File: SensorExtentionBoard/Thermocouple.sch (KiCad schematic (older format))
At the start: 9 parts, among them J301 Conn_01x02_Male, J302 Conn_01x02_Male, U301 MCP4728, U302 TS3A24159DGSR, U303 TS3A24159DGSR

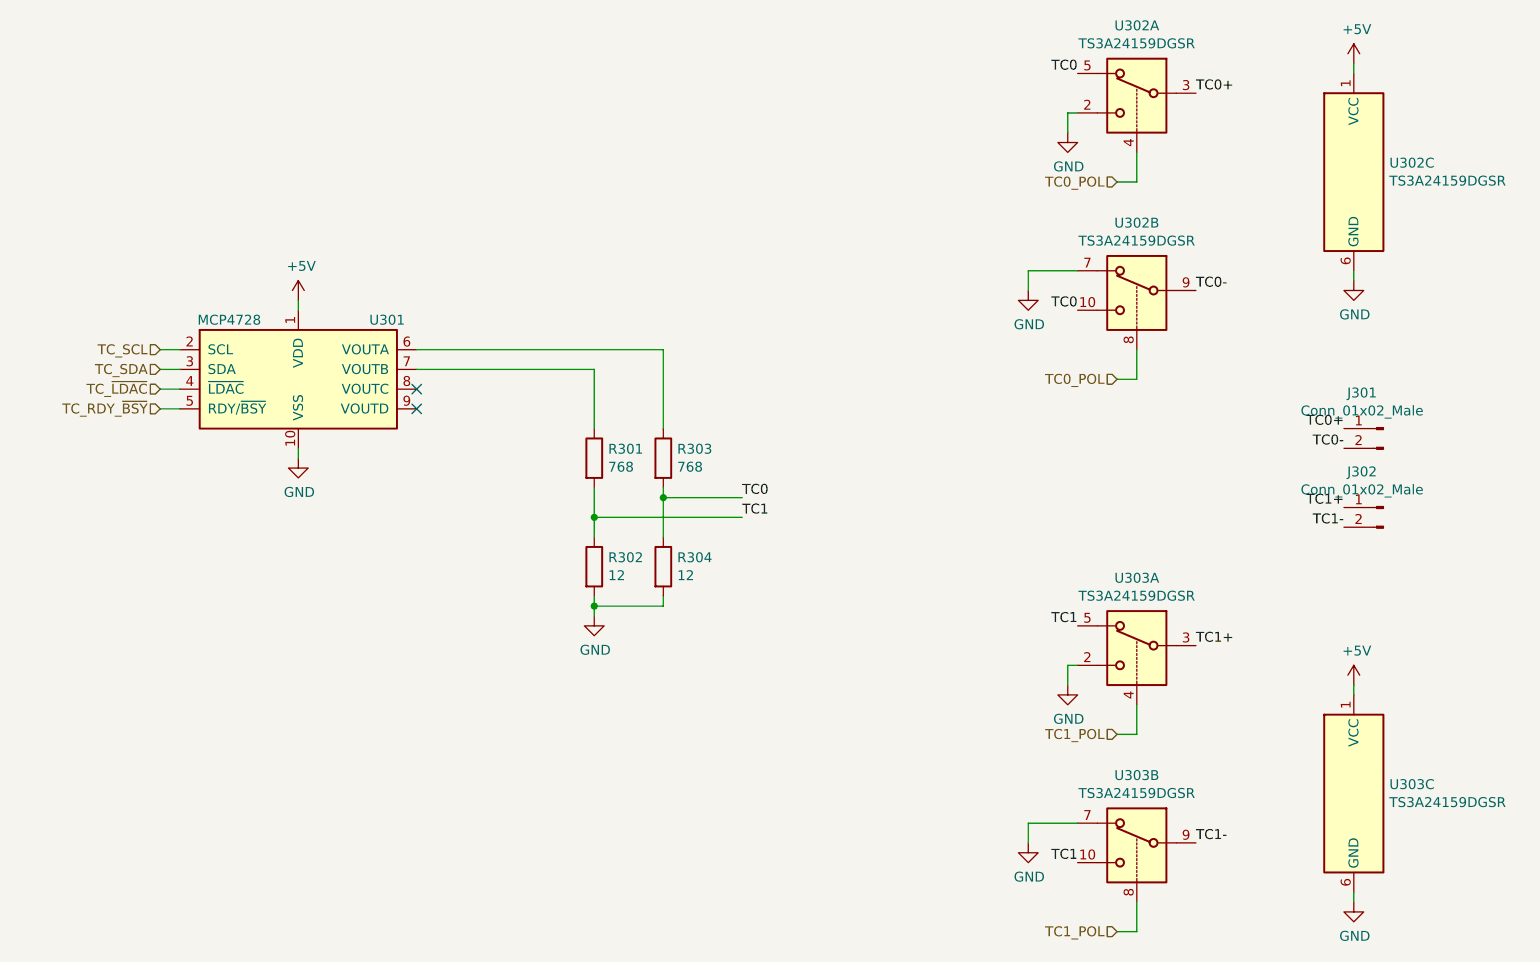
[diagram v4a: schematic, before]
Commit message: Added header for programming the EEPROM memory on the SEB
Adding this header may allow the test rig to load new memory configs
onto the SEB under test prior to running tests. This will allow
greater ability for automation of testing when the new software
requires a change to the config onboard the SEB.
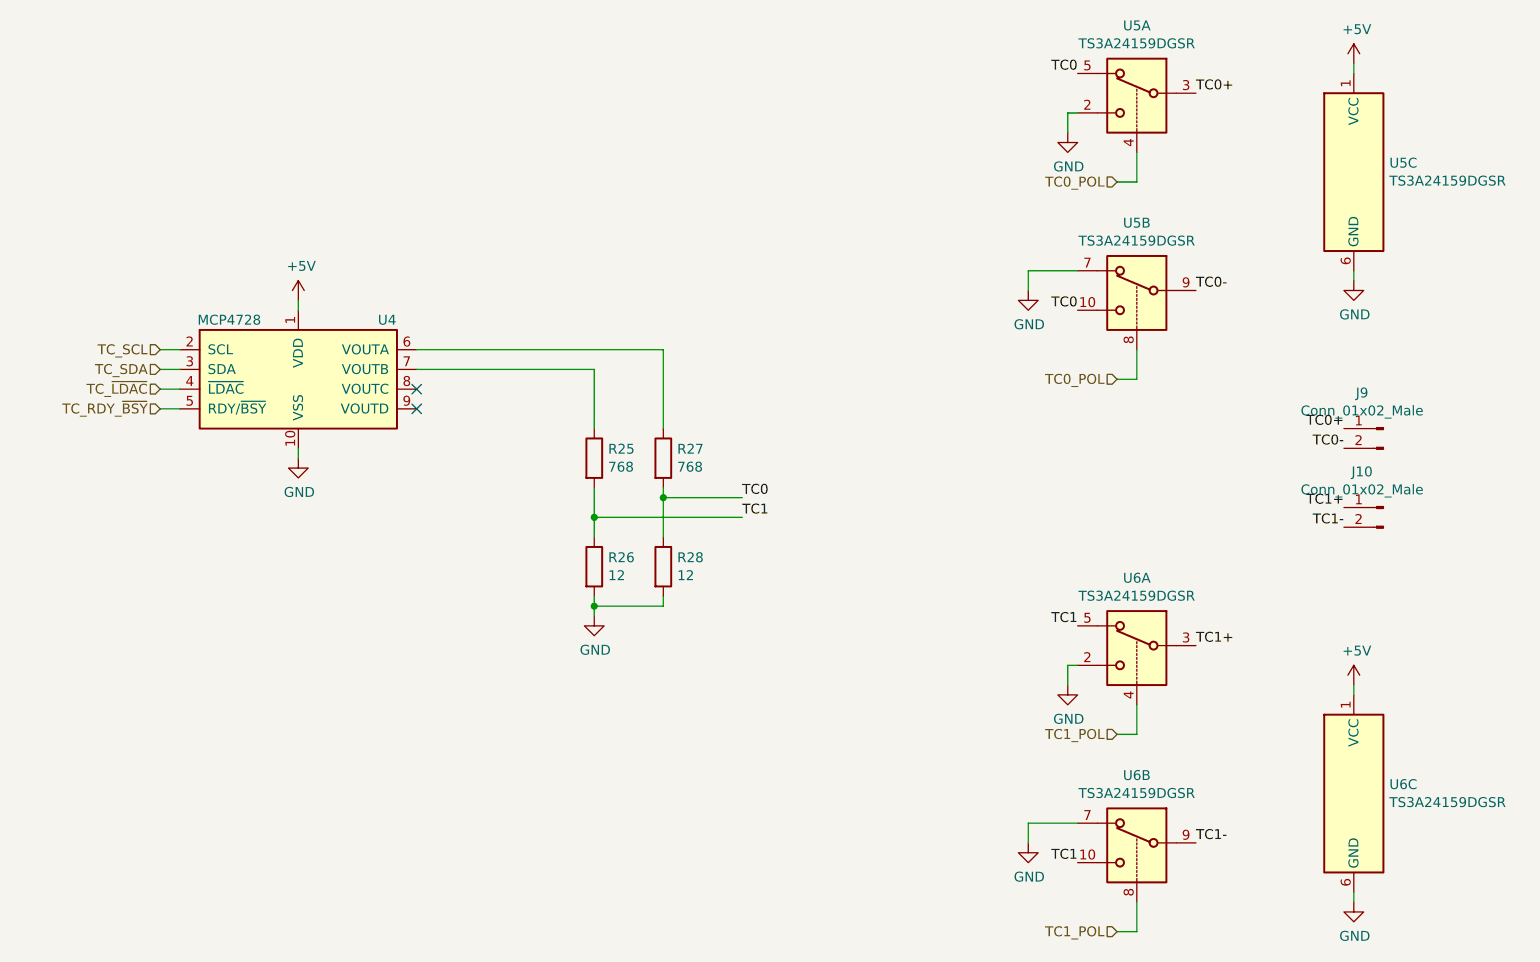
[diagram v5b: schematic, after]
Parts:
- renumbered J302 to J10, J301 to J9, R301 to R25, R302 to R26, R303 to R27, R304 to R28, U301 to U4, U302 to U5, U303 to U6
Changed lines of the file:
@@
 $EndDescr
 $Comp
-L Analog_DAC:MCP4728 U301
+L Analog_DAC:MCP4728 U4
 U 1 1 5E2FD865
 P 4000 2350
-F 0 "U301" H 4450 2600 50  0000 C CNN
+F 0 "U4" H 4450 2600 50  0000 C CNN
 F 1 "MCP4728" H 3650 2600 50  0000 C CNN
 F 2 "Package_SO:MSOP-10_3x3mm_P0.5mm" H 4000 1750 50  0001 C CNN
@@
 $EndComp
 $Comp
-L power:GND #PWR0302
+L power:GND #PWR028
 U 1 1 5E2FE6B0
 P 4000 2800
-F 0 "#PWR0302" H 4000 2550 50  0001 C CNN
+F 0 "#PWR028" H 4000 2550 50  0001 C CNN
 F 1 "GND" H 4005 2627 50  0000 C CNN
 F 2 "" H 4000 2800 50  0001 C CNN
@@
 	4000 2800 4000 2750
 $Comp
-L power:+5V #PWR0301
+L power:+5V #PWR027
 U 1 1 5E2FE9D8
 P 4000 2000
-F 0 "#PWR0301" H 4000 1850 50  0001 C CNN
+F 0 "#PWR027" H 4000 1850 50  0001 C CNN
 F 1 "+5V" H 4015 2173 50  0000 C CNN
 F 2 "" H 4000 2000 50  0001 C CNN
@@
 	3300 2450 3400 2450
 $Comp
-L Device:R R303
+L Device:R R27
 U 1 1 5E3006EF
 P 5850 2800
-F 0 "R303" H 5920 2846 50  0000 L CNN
+F 0 "R27" H 5920 2846 50  0000 L CNN
 F 1 "768" H 5920 2755 50  0000 L CNN
 F 2 "Resistor_SMD:R_1206_3216Metric_Pad1.42x1.75mm_HandSolder" V 5780 2800 50  0001 C CNN
@@
 $EndComp
 $Comp
-L Device:R R304
+L Device:R R28
 U 1 1 5E300948
 P 5850 3350
-F 0 "R304" H 5920 3396 50  0000 L CNN
+F 0 "R28" H 5920 3396 50  0000 L CNN
 F 1 "12" H 5920 3305 50  0000 L CNN
 F 2 "Resistor_SMD:R_1206_3216Metric_Pad1.42x1.75mm_HandSolder" V 5780 3350 50  0001 C CNN
@@
 $EndComp
 $Comp
-L Device:R R301
+L Device:R R25
 U 1 1 5E3082B4
 P 5500 2800
-F 0 "R301" H 5570 2846 50  0000 L CNN
+F 0 "R25" H 5570 2846 50  0000 L CNN
 F 1 "768" H 5570 2755 50  0000 L CNN
 F 2 "Resistor_SMD:R_1206_3216Metric_Pad1.42x1.75mm_HandSolder" V 5430 2800 50  0001 C CNN
@@
 $EndComp
 $Comp
-L Device:R R302
+L Device:R R26
 U 1 1 5E3082BA
 P 5500 3350
-F 0 "R302" H 5570 3396 50  0000 L CNN
+F 0 "R26" H 5570 3396 50  0000 L CNN
 F 1 "12" H 5570 3305 50  0000 L CNN
 F 2 "Resistor_SMD:R_1206_3216Metric_Pad1.42x1.75mm_HandSolder" V 5430 3350 50  0001 C CNN
@@
 	5500 3100 5500 3200
 $Comp
-L power:GND #PWR0303
+L power:GND #PWR029
 U 1 1 5E3159B6
 P 5500 3600
-F 0 "#PWR0303" H 5500 3350 50  0001 C CNN
+F 0 "#PWR029" H 5500 3350 50  0001 C CNN
 F 1 "GND" H 5505 3427 50  0000 C CNN
 F 2 "" H 5500 3600 50  0001 C CNN
@@
 NoConn ~ 4600 2450
 $Comp
-L Analog_Switch:TS3A24159DGSR U302
+L Analog_Switch:TS3A24159DGSR U5
 U 3 1 5E318CFB
 P 9350 1350
-F 0 "U302" H 9530 1396 50  0000 L CNN
+F 0 "U5" H 9530 1396 50  0000 L CNN
 F 1 "TS3A24159DGSR" H 9530 1305 50  0000 L CNN
 F 2 "Package_SO:TSSOP-10_3x3mm_P0.5mm" H 9350 1000 50  0001 C CNN
@@
 $EndComp
 $Comp
-L power:+5V #PWR0308
+L power:+5V #PWR034
 U 1 1 5E33134D
 P 9350 800
-F 0 "#PWR0308" H 9350 650 50  0001 C CNN
+F 0 "#PWR034" H 9350 650 50  0001 C CNN
 F 1 "+5V" H 9365 973 50  0000 C CNN
 F 2 "" H 9350 800 50  0001 C CNN
@@
 	9350 800  9350 850
 $Comp
-L power:GND #PWR0309
+L power:GND #PWR035
 U 1 1 5E332A5C
 P 9350 1900
-F 0 "#PWR0309" H 9350 1650 50  0001 C CNN
+F 0 "#PWR035" H 9350 1650 50  0001 C CNN
 F 1 "GND" H 9355 1727 50  0000 C CNN
 F 2 "" H 9350 1900 50  0001 C CNN
@@
 TC0
 $Comp
-L power:GND #PWR0304
+L power:GND #PWR030
 U 1 1 5E324555
 P 7700 1950
-F 0 "#PWR0304" H 7700 1700 50  0001 C CNN
+F 0 "#PWR030" H 7700 1700 50  0001 C CNN
 F 1 "GND" H 7705 1777 50  0000 C CNN
 F 2 "" H 7700 1950 50  0001 C CNN
@@
 $EndComp
 $Comp
-L power:GND #PWR0306
+L power:GND #PWR032
 U 1 1 5E324066
 P 7900 1150
-F 0 "#PWR0306" H 7900 900 50  0001 C CNN
+F 0 "#PWR032" H 7900 900 50  0001 C CNN
 F 1 "GND" H 7905 977 50  0000 C CNN
 F 2 "" H 7900 1150 50  0001 C CNN
@@
 TC0+
 $Comp
-L Analog_Switch:TS3A24159DGSR U302
+L Analog_Switch:TS3A24159DGSR U5
 U 2 1 5E317F40
 P 8250 1850
-F 0 "U302" H 8250 2092 50  0000 C CNN
+F 0 "U5" H 8250 2092 50  0000 C CNN
 F 1 "TS3A24159DGSR" H 8250 2001 50  0000 C CNN
 F 2 "Package_SO:TSSOP-10_3x3mm_P0.5mm" H 8250 1500 50  0001 C CNN
@@
 $EndComp
 $Comp
-L Analog_Switch:TS3A24159DGSR U302
+L Analog_Switch:TS3A24159DGSR U5
 U 1 1 5E31745F
 P 8250 850
-F 0 "U302" H 8250 1092 50  0000 C CNN
+F 0 "U5" H 8250 1092 50  0000 C CNN
 F 1 "TS3A24159DGSR" H 8250 1001 50  0000 C CNN
 F 2 "Package_SO:TSSOP-10_3x3mm_P0.5mm" H 8250 500 50  0001 C CNN
@@
 $EndComp
 $Comp
-L Analog_Switch:TS3A24159DGSR U303
+L Analog_Switch:TS3A24159DGSR U6
 U 3 1 5E35C1F5
 P 9350 4500
-F 0 "U303" H 9530 4546 50  0000 L CNN
+F 0 "U6" H 9530 4546 50  0000 L CNN
 F 1 "TS3A24159DGSR" H 9530 4455 50  0000 L CNN
 F 2 "Package_SO:TSSOP-10_3x3mm_P0.5mm" H 9350 4150 50  0001 C CNN
@@
 $EndComp
 $Comp
-L power:+5V #PWR0310
+L power:+5V #PWR036
 U 1 1 5E35C1FB
 P 9350 3950
-F 0 "#PWR0310" H 9350 3800 50  0001 C CNN
+F 0 "#PWR036" H 9350 3800 50  0001 C CNN
 F 1 "+5V" H 9365 4123 50  0000 C CNN
 F 2 "" H 9350 3950 50  0001 C CNN
@@
 	9350 3950 9350 4000
 $Comp
-L power:GND #PWR0311
+L power:GND #PWR037
 U 1 1 5E35C202
 P 9350 5050
-F 0 "#PWR0311" H 9350 4800 50  0001 C CNN
+F 0 "#PWR037" H 9350 4800 50  0001 C CNN
 F 1 "GND" H 9355 4877 50  0000 C CNN
 F 2 "" H 9350 5050 50  0001 C CNN
@@
 TC1
 $Comp
-L power:GND #PWR0305
+L power:GND #PWR031
 U 1 1 5E35C215
 P 7700 4750
-F 0 "#PWR0305" H 7700 4500 50  0001 C CNN
+F 0 "#PWR031" H 7700 4500 50  0001 C CNN
 F 1 "GND" H 7705 4577 50  0000 C CNN
 F 2 "" H 7700 4750 50  0001 C CNN
@@
 $EndComp
 $Comp
-L power:GND #PWR0307
+L power:GND #PWR033
 U 1 1 5E35C21B
 P 7900 3950
-F 0 "#PWR0307" H 7900 3700 50  0001 C CNN
+F 0 "#PWR033" H 7900 3700 50  0001 C CNN
 F 1 "GND" H 7905 3777 50  0000 C CNN
 F 2 "" H 7900 3950 50  0001 C CNN
@@
 TC1+
 $Comp
-L Analog_Switch:TS3A24159DGSR U303
+L Analog_Switch:TS3A24159DGSR U6
 U 2 1 5E35C223
 P 8250 4650
-F 0 "U303" H 8250 4892 50  0000 C CNN
+F 0 "U6" H 8250 4892 50  0000 C CNN
 F 1 "TS3A24159DGSR" H 8250 4801 50  0000 C CNN
 F 2 "Package_SO:TSSOP-10_3x3mm_P0.5mm" H 8250 4300 50  0001 C CNN
@@
 $EndComp
 $Comp
-L Analog_Switch:TS3A24159DGSR U303
+L Analog_Switch:TS3A24159DGSR U6
 U 1 1 5E35C229
 P 8250 3650
-F 0 "U303" H 8250 3892 50  0000 C CNN
+F 0 "U6" H 8250 3892 50  0000 C CNN
 F 1 "TS3A24159DGSR" H 8250 3801 50  0000 C CNN
 F 2 "Package_SO:TSSOP-10_3x3mm_P0.5mm" H 8250 3300 50  0001 C CNN
@@
 $EndComp
 $Comp
-L Connector:Conn_01x02_Male J301
+L Connector:Conn_01x02_Male J9
 U 1 1 5E388A81
 P 9500 2650
-F 0 "J301" H 9608 2831 50  0000 C CNN
+F 0 "J9" H 9608 2831 50  0000 C CNN
 F 1 "Conn_01x02_Male" H 9608 2740 50  0000 C CNN
 F 2 "Connector_Molex:Molex_MicroClasp_55932-0210_1x02_P2.00mm_Vertical" H 9500 2650 50  0001 C CNN
@@
 $EndComp
 $Comp
-L Connector:Conn_01x02_Male J302
+L Connector:Conn_01x02_Male J10
 U 1 1 5E391340
 P 9500 3050
-F 0 "J302" H 9608 3231 50  0000 C CNN
+F 0 "J10" H 9608 3231 50  0000 C CNN
 F 1 "Conn_01x02_Male" H 9608 3140 50  0000 C CNN
 F 2 "Connector_Molex:Molex_MicroClasp_55932-0210_1x02_P2.00mm_Vertical" H 9500 3050 50  0001 C CNN

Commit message: Changed component footprints to conform to RP standard components
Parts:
- J10, J9: footprint Connector_Molex:Molex_MicroClasp_55932-0210_1x02_P2.00mm_Vertical -> Connector_Molex:Molex_MicroClasp_55932-0230_1x02_P2.00mm_Vertical
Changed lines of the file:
@@
 encoding utf-8
 Sheet 3 5
-Title ""
-Date ""
-Rev ""
-Comp ""
-Comment1 ""
+Title "Helix Test Rig SEB"
+Date "2020-01-14"
+Rev "1.0.0"
+Comp "SDSU Rocket Project"
+Comment1 "Schematic Design: David Knight"
 Comment2 ""
 Comment3 ""
@@
 $EndComp
 $Comp
-L power:GND #PWR028
+L power:GND #PWR031
 U 1 1 5E2FE6B0
 P 4000 2800
-F 0 "#PWR028" H 4000 2550 50  0001 C CNN
+F 0 "#PWR031" H 4000 2550 50  0001 C CNN
 F 1 "GND" H 4005 2627 50  0000 C CNN
 F 2 "" H 4000 2800 50  0001 C CNN
@@
 	4000 2800 4000 2750
 $Comp
-L power:+5V #PWR027
+L power:+5V #PWR030
 U 1 1 5E2FE9D8
 P 4000 2000
-F 0 "#PWR027" H 4000 1850 50  0001 C CNN
+F 0 "#PWR030" H 4000 1850 50  0001 C CNN
 F 1 "+5V" H 4015 2173 50  0000 C CNN
 F 2 "" H 4000 2000 50  0001 C CNN
@@
 	5500 3100 5500 3200
 $Comp
-L power:GND #PWR029
+L power:GND #PWR032
 U 1 1 5E3159B6
 P 5500 3600
-F 0 "#PWR029" H 5500 3350 50  0001 C CNN
+F 0 "#PWR032" H 5500 3350 50  0001 C CNN
 F 1 "GND" H 5505 3427 50  0000 C CNN
 F 2 "" H 5500 3600 50  0001 C CNN
@@
 $EndComp
 $Comp
-L power:+5V #PWR034
+L power:+5V #PWR037
 U 1 1 5E33134D
 P 9350 800
-F 0 "#PWR034" H 9350 650 50  0001 C CNN
+F 0 "#PWR037" H 9350 650 50  0001 C CNN
 F 1 "+5V" H 9365 973 50  0000 C CNN
 F 2 "" H 9350 800 50  0001 C CNN
@@
 	9350 800  9350 850
 $Comp
-L power:GND #PWR035
+L power:GND #PWR038
 U 1 1 5E332A5C
 P 9350 1900
-F 0 "#PWR035" H 9350 1650 50  0001 C CNN
+F 0 "#PWR038" H 9350 1650 50  0001 C CNN
 F 1 "GND" H 9355 1727 50  0000 C CNN
 F 2 "" H 9350 1900 50  0001 C CNN
@@
 TC0
 $Comp
-L power:GND #PWR030
+L power:GND #PWR033
 U 1 1 5E324555
 P 7700 1950
-F 0 "#PWR030" H 7700 1700 50  0001 C CNN
+F 0 "#PWR033" H 7700 1700 50  0001 C CNN
 F 1 "GND" H 7705 1777 50  0000 C CNN
 F 2 "" H 7700 1950 50  0001 C CNN
@@
 $EndComp
 $Comp
-L power:GND #PWR032
+L power:GND #PWR035
 U 1 1 5E324066
 P 7900 1150
-F 0 "#PWR032" H 7900 900 50  0001 C CNN
+F 0 "#PWR035" H 7900 900 50  0001 C CNN
 F 1 "GND" H 7905 977 50  0000 C CNN
 F 2 "" H 7900 1150 50  0001 C CNN
@@
 $EndComp
 $Comp
-L power:+5V #PWR036
+L power:+5V #PWR039
 U 1 1 5E35C1FB
 P 9350 3950
-F 0 "#PWR036" H 9350 3800 50  0001 C CNN
+F 0 "#PWR039" H 9350 3800 50  0001 C CNN
 F 1 "+5V" H 9365 4123 50  0000 C CNN
 F 2 "" H 9350 3950 50  0001 C CNN
@@
 	9350 3950 9350 4000
 $Comp
-L power:GND #PWR037
+L power:GND #PWR040
 U 1 1 5E35C202
 P 9350 5050
-F 0 "#PWR037" H 9350 4800 50  0001 C CNN
+F 0 "#PWR040" H 9350 4800 50  0001 C CNN
 F 1 "GND" H 9355 4877 50  0000 C CNN
 F 2 "" H 9350 5050 50  0001 C CNN
@@
 TC1
 $Comp
-L power:GND #PWR031
+L power:GND #PWR034
 U 1 1 5E35C215
 P 7700 4750
-F 0 "#PWR031" H 7700 4500 50  0001 C CNN
+F 0 "#PWR034" H 7700 4500 50  0001 C CNN
 F 1 "GND" H 7705 4577 50  0000 C CNN
 F 2 "" H 7700 4750 50  0001 C CNN
@@
 $EndComp
 $Comp
-L power:GND #PWR033
+L power:GND #PWR036
 U 1 1 5E35C21B
 P 7900 3950
-F 0 "#PWR033" H 7900 3700 50  0001 C CNN
+F 0 "#PWR036" H 7900 3700 50  0001 C CNN
 F 1 "GND" H 7905 3777 50  0000 C CNN
 F 2 "" H 7900 3950 50  0001 C CNN
@@
 F 0 "J9" H 9608 2831 50  0000 C CNN
 F 1 "Conn_01x02_Male" H 9608 2740 50  0000 C CNN
-F 2 "Connector_Molex:Molex_MicroClasp_55932-0210_1x02_P2.00mm_Vertical" H 9500 2650 50  0001 C CNN
+F 2 "Connector_Molex:Molex_MicroClasp_55932-0230_1x02_P2.00mm_Vertical" H 9500 2650 50  0001 C CNN
 F 3 "~" H 9500 2650 50  0001 C CNN
 	1    9500 2650
@@
 F 0 "J10" H 9608 3231 50  0000 C CNN
 F 1 "Conn_01x02_Male" H 9608 3140 50  0000 C CNN
-F 2 "Connector_Molex:Molex_MicroClasp_55932-0210_1x02_P2.00mm_Vertical" H 9500 3050 50  0001 C CNN
+F 2 "Connector_Molex:Molex_MicroClasp_55932-0230_1x02_P2.00mm_Vertical" H 9500 3050 50  0001 C CNN
 F 3 "~" H 9500 3050 50  0001 C CNN
 	1    9500 3050
